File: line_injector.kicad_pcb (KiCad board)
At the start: 2 copper layers, 120 x 100 mm, 21 parts, among them J1 Conn_01x01_Female, J2 Conn_01x01_Female, J3 Conn_01x01_Female, J4 Conn_01x01_Female, J5 Conn_01x01_Female, J6 Conn_01x01_Female, J7 Conn_Coaxial, Q1 AOT2618

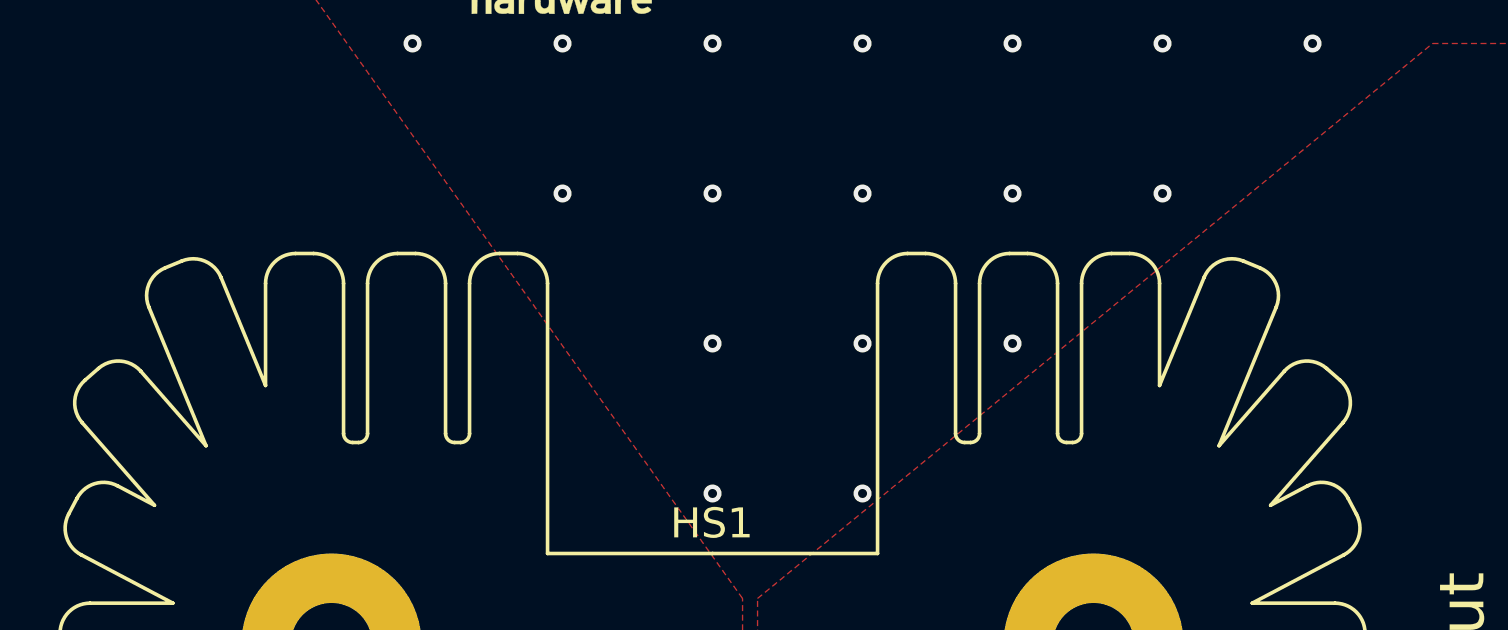
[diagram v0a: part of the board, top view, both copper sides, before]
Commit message: Added RoHS info
Added temperature data
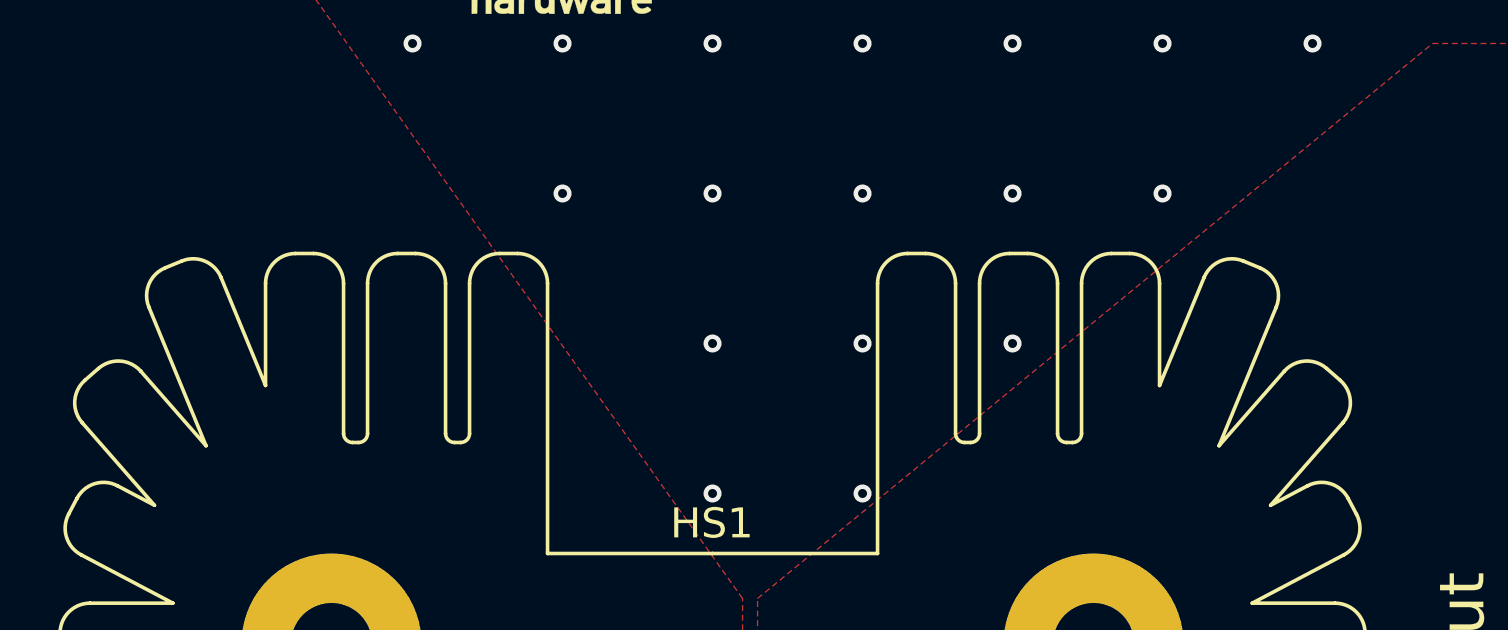
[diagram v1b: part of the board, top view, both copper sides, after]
